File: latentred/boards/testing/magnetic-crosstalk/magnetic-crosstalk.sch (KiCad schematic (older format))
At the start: 89 parts, among them J1 STEWART_SS_74500_024, J2 SMA, J3 SMA, J4 SMA, J5 SMA, J6 SMA, J7 SMA, J8 SMA, J9 SMA

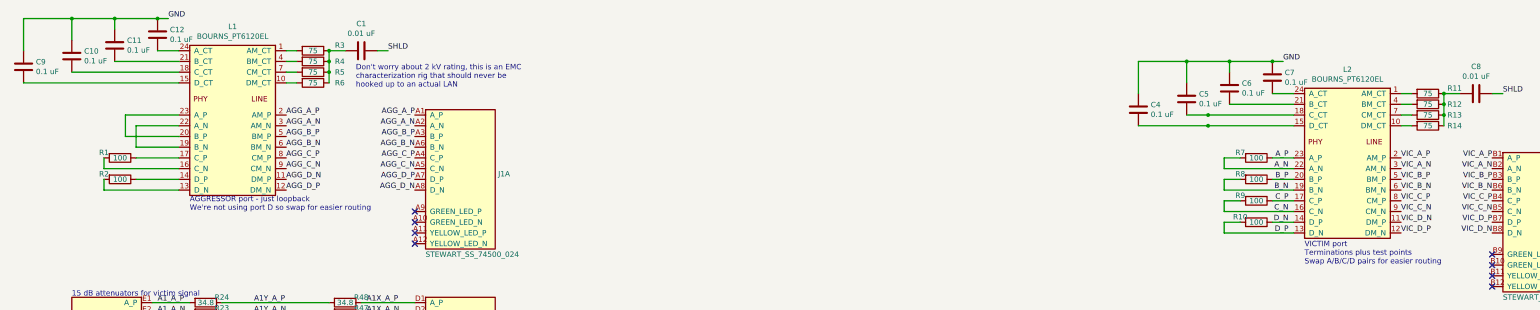
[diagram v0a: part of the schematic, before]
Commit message: Fixed pinout bugs. v0.2 PCB release.
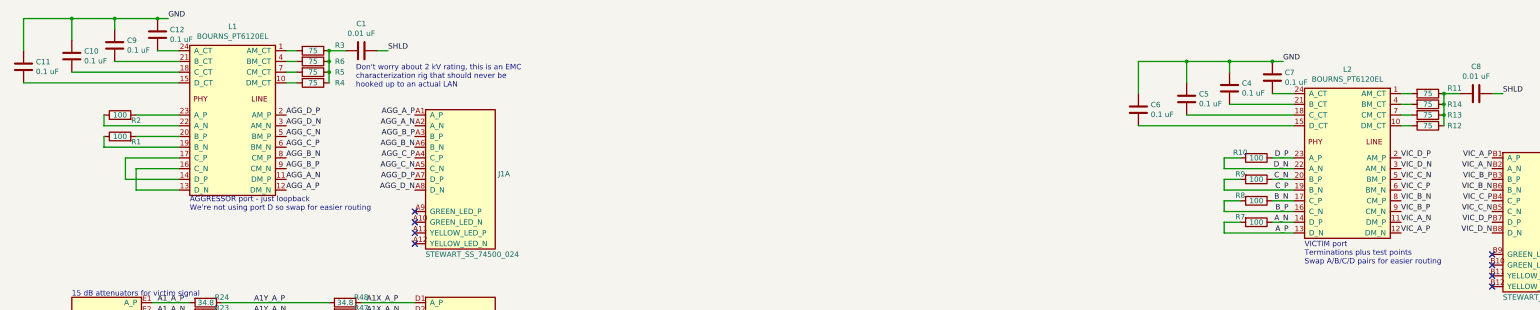
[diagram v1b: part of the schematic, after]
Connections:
- net AGG_A_N: now also L1.11 (DM_P); no longer L1.3 (AM_N)
- net AGG_A_P: now also L1.12 (DM_N); no longer L1.2 (AM_P)
- net AGG_B_N: now also L1.8 (CM_P); no longer L1.6 (BM_N)
- net AGG_B_P: now also L1.9 (CM_N); no longer L1.5 (BM_P)
- net AGG_C_N: now also L1.5 (BM_P); no longer L1.9 (CM_N)
- net AGG_C_P: now also L1.6 (BM_N); no longer L1.8 (CM_P)
- net AGG_D_N: now also L1.3 (AM_N); no longer L1.11 (DM_P)
- net AGG_D_P: now also L1.2 (AM_P); no longer L1.12 (DM_N)
- net A_N: now also L2.14 (D_P), R7.1; no longer L2.22 (A_N), R7.2
- net A_P: now also L2.13 (D_N), R7.2; no longer L2.23 (A_P), R7.1
- net B_N: now also L2.17 (C_P), R8.1; no longer L2.19 (B_N), R8.2
- net B_P: now also L2.16 (C_N), R8.2; no longer L2.20 (B_P), R8.1
- net C_N: now also L2.20 (B_P), R9.1; no longer L2.16 (C_N), R9.2
- net C_P: now also L2.19 (B_N), R9.2; no longer L2.17 (C_P), R9.1
- net D_N: now also L2.22 (A_N), R10.2; no longer L2.14 (D_P), R10.1
- net D_P: now also L2.23 (A_P), R10.1; no longer L2.13 (D_N), R10.2
- net VIC_A_N: now also L2.11 (DM_P); no longer L2.3 (AM_N)
- net VIC_A_P: now also L2.12 (DM_N); no longer L2.2 (AM_P)
- net VIC_B_N: now also L2.8 (CM_P); no longer L2.6 (BM_N)
- net VIC_B_P: now also L2.9 (CM_N); no longer L2.5 (BM_P)
- net VIC_C_N: now also L2.5 (BM_P); no longer L2.9 (CM_N)
- net VIC_C_P: now also L2.6 (BM_N); no longer L2.8 (CM_P)
- net VIC_D_N: now also L2.3 (AM_N); no longer L2.11 (DM_P)
- net VIC_D_P: now also L2.2 (AM_P); no longer L2.12 (DM_N)
- net at L1.10 (DM_CT): now also R4.2; no longer R6.2
- net at L1.13 (D_N): now also L1.16 (C_N); no longer R2.2
- net at L1.14 (D_P): now also L1.17 (C_P); no longer R2.1
- net at L1.15 (D_CT): now also C11.2; no longer C9.2
- net at R1.2: now also L1.20 (B_P); no longer L1.16 (C_N)
- net at R1.1: now also L1.19 (B_N); no longer L1.17 (C_P)
- net at L1.22 (A_N): now also R2.1; no longer L1.19 (B_N)
- net at L1.23 (A_P): now also R2.2; no longer L1.20 (B_P)
- net at L1.21 (B_CT): now also C9.2; no longer C11.2
- net at L1.4 (BM_CT): now also R6.2; no longer R4.2
- net at L2.10 (DM_CT): now also R12.2; no longer R14.2
- net at L2.15 (D_CT): now also C6.2; no longer C4.2
- net at L2.21 (B_CT): now also C4.2; no longer C6.2
- net at L2.4 (BM_CT): now also R14.2; no longer R12.2
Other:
- moved on the sheet: C11, C4, C6, C9, R1, R10, R12, R14, R2, R4, R6, R7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

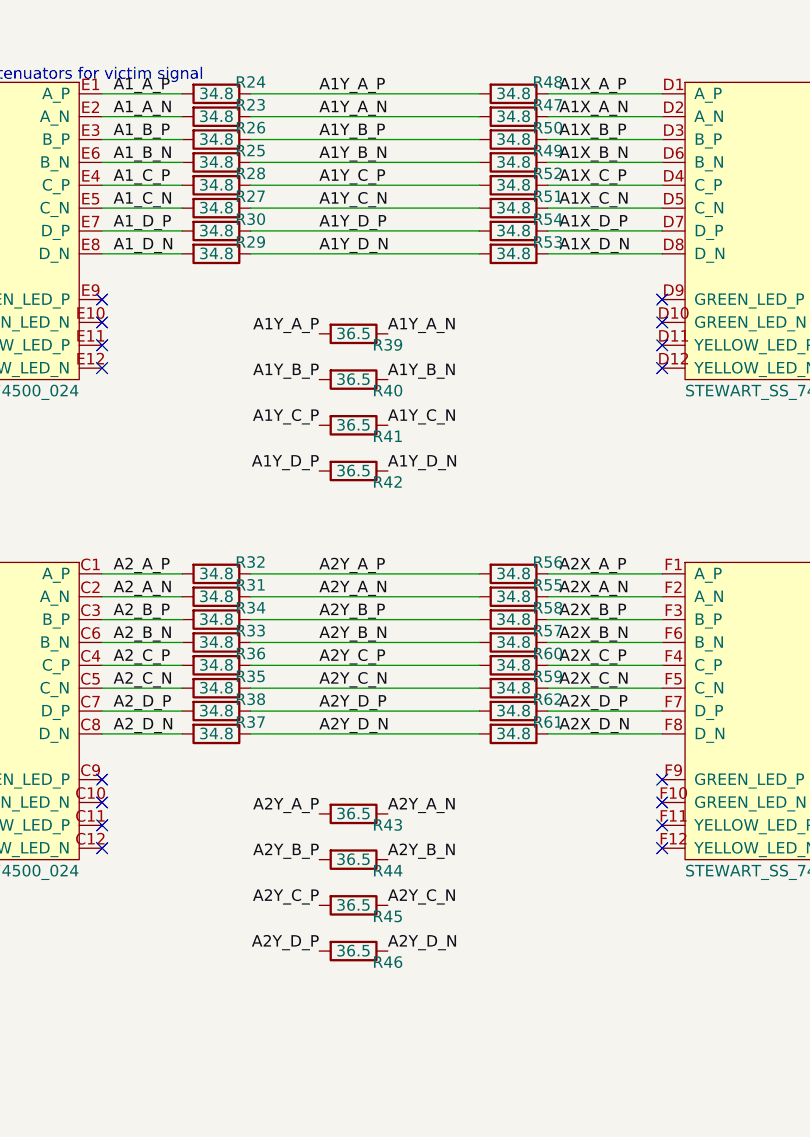
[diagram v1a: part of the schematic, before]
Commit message: Updated magnetic-crosstalk to v0.3 respin
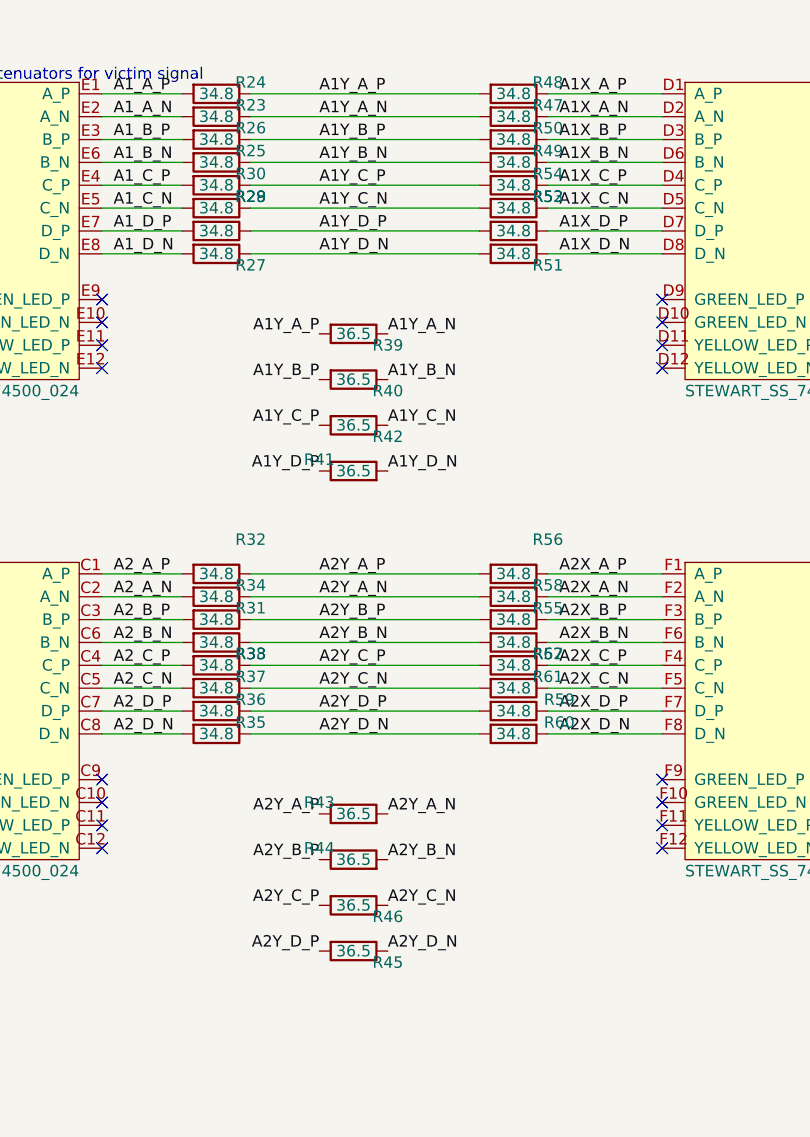
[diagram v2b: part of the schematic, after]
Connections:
- net A1X_C_N: now also R54.1; no longer R52.1
- net A1X_C_P: now also R53.1; no longer R51.1
- net A1X_D_N: now also R51.1; no longer R54.1
- net A1X_D_P: now also R52.1; no longer R53.1
- net A1Y_C_N: now also R30.1, R42.1, R54.2; no longer R28.1, R41.1, R52.2
- net A1Y_C_P: now also R29.1, R42.2, R53.2; no longer R27.1, R41.2, R51.2
- net A1Y_D_N: now also R27.1, R41.2, R51.2; no longer R30.1, R42.1, R54.2
- net A1Y_D_P: now also R28.1, R41.1, R52.2; no longer R29.1, R42.2, R53.2
- net A1_C_N: now also R30.2; no longer R28.2
- net A1_C_P: now also R29.2; no longer R27.2
- net A1_D_N: now also R27.2; no longer R30.2
- net A1_D_P: now also R28.2; no longer R29.2
- net A2X_A_N: now also R55.1; no longer R56.1
- net A2X_A_P: now also R56.1; no longer R55.1
- net A2X_B_N: now also R57.1; no longer R58.1
- net A2X_B_P: now also R58.1; no longer R57.1
- net A2X_C_N: now also R62.1; no longer R60.1
- net A2X_C_P: now also R61.1; no longer R59.1
- net A2X_D_N: now also R60.1; no longer R62.1
- net A2X_D_P: now also R59.1; no longer R61.1
- net A2Y_A_N: now also R31.1, R43.2, R55.2; no longer R32.1, R43.1, R56.2
- net A2Y_A_P: now also R32.1, R43.1, R56.2; no longer R31.1, R43.2, R55.2
- net A2Y_B_N: now also R33.1, R44.2, R57.2; no longer R34.1, R44.1, R58.2
- net A2Y_B_P: now also R34.1, R44.1, R58.2; no longer R33.1, R44.2, R57.2
- net A2Y_C_N: now also R38.1, R46.1, R62.2; no longer R36.1, R45.1, R60.2
- net A2Y_C_P: now also R37.1, R46.2, R61.2; no longer R35.1, R45.2, R59.2
- net A2Y_D_N: now also R36.1, R45.1, R60.2; no longer R38.1, R46.1, R62.2
- net A2Y_D_P: now also R35.1, R45.2, R59.2; no longer R37.1, R46.2, R61.2
- net A2_A_N: now also R31.2; no longer R32.2
- net A2_A_P: now also R32.2; no longer R31.2
- net A2_B_N: now also R33.2; no longer R34.2
- net A2_B_P: now also R34.2; no longer R33.2
- net A2_C_N: now also R38.2; no longer R36.2
- net A2_C_P: now also R37.2; no longer R35.2
- net A2_D_N: now also R36.2; no longer R38.2
- net A2_D_P: now also R35.2; no longer R37.2
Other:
- moved on the sheet: R27, R28, R29, R30, R31, R32, R33, R34, R35, R36, R37, R38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
